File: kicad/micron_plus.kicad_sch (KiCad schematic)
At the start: 0 parts

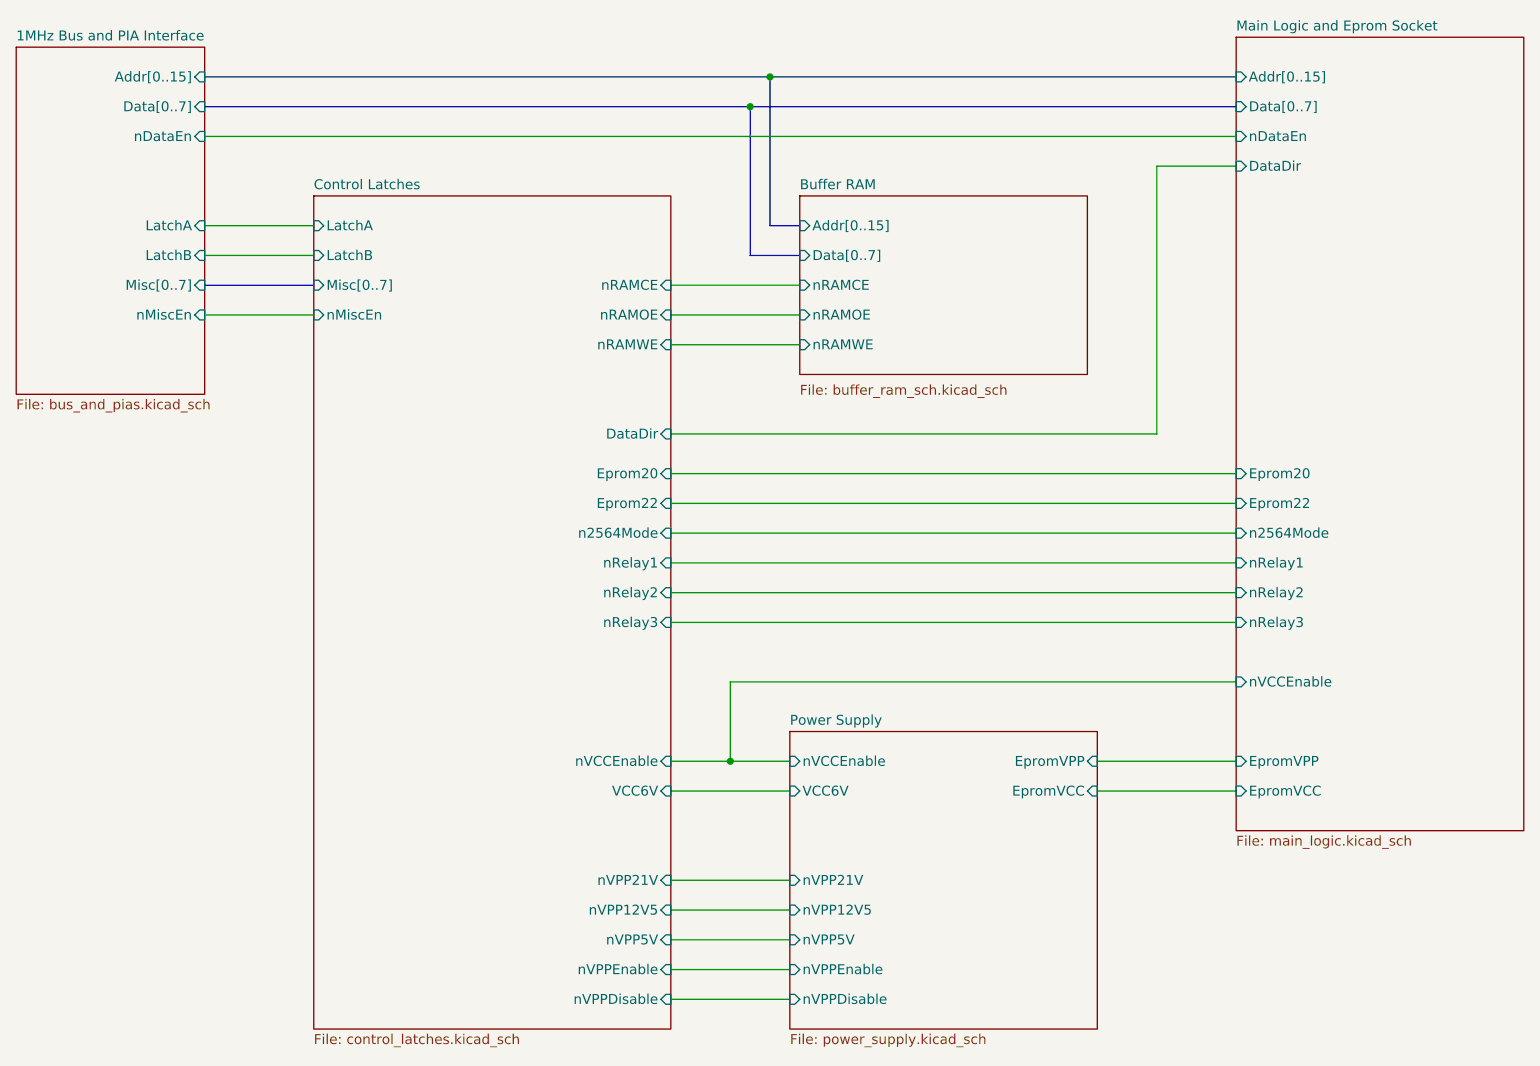
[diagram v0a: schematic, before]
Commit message: Move 7406 onto PSU sheet
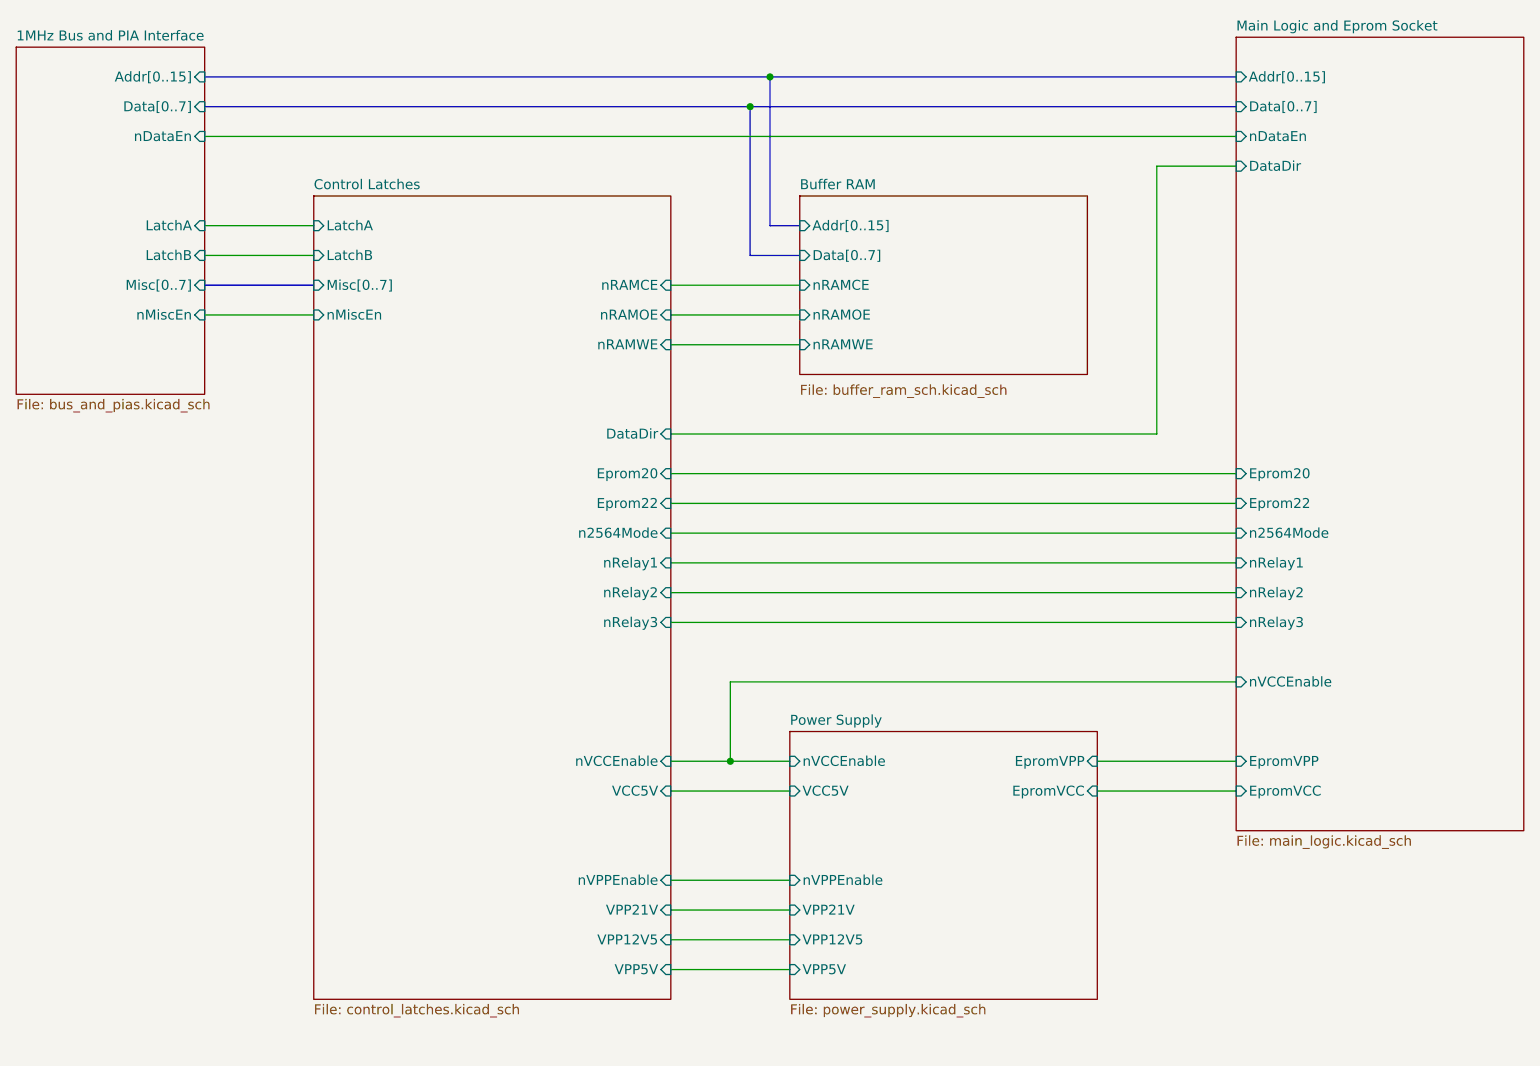
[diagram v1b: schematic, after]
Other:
- sheet Control Latches ports: added VCC5V, VPP12V5, VPP21V, VPP5V; removed VCC6V, nVPP12V5, nVPP21V, nVPP5V, nVPPDisable
- sheet Power Supply ports: added VCC5V, VPP12V5, VPP21V, VPP5V; removed VCC6V, nVPP12V5, nVPP21V, nVPP5V, nVPPDisable
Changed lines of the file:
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@@
-    (stroke (width 0) (type default) (color 0 0 0 0))
-  )
-  (wire (pts (xy 138.43 153.67) (xy 153.67 153.67))
     (stroke (width 0) (type default) (color 0 0 0 0))
   )
@@
     )
   )
-  (sheet (at 92.71 50.8) (size 45.72 106.68) (fields_autoplaced)
+  (sheet (at 92.71 50.8) (size 45.72 102.87) (fields_autoplaced)
     (stroke (width 0.1524) (type solid) (color 0 0 0 0))
     (fill (color 0 0 0 0.0000))
@@
       (effects (font (size 1.27 1.27)) (justify left bottom))
     )
-    (property "Sheet file" "control_latches.kicad_sch" (id 1) (at 92.71 158.0646 0)
+    (property "Sheet file" "control_latches.kicad_sch" (id 1) (at 92.71 154.2546 0)
       (effects (font (size 1.27 1.27)) (justify left top))
     )
@@
       (effects (font (size 1.27 1.27)) (justify right))
     )
-    (pin "nVPPEnable" input (at 138.43 149.86 0)
-      (effects (font (size 1.27 1.27)) (justify right))
-    )
     (pin "LatchB" input (at 92.71 58.42 180)
       (effects (font (size 1.27 1.27)) (justify left))
@@
       (effects (font (size 1.27 1.27)) (justify left))
     )
-    (pin "nVPPDisable" input (at 138.43 153.67 0)
-      (effects (font (size 1.27 1.27)) (justify right))
-    )
     (pin "nVCCEnable" input (at 138.43 123.19 0)
       (effects (font (size 1.27 1.27)) (justify right))
     )
-    (pin "nVPP12V5" input (at 138.43 142.24 0)
-      (effects (font (size 1.27 1.27)) (justify right))
-    )
-    (pin "nVPP21V" input (at 138.43 138.43 0)
-      (effects (font (size 1.27 1.27)) (justify right))
-    )
     (pin "nRelay3" input (at 138.43 105.41 0)
       (effects (font (size 1.27 1.27)) (justify right))
@@
       (effects (font (size 1.27 1.27)) (justify right))
     )
-    (pin "VCC6V" input (at 138.43 127 0)
-      (effects (font (size 1.27 1.27)) (justify right))
-    )
-    (pin "nVPP5V" input (at 138.43 146.05 0)
-      (effects (font (size 1.27 1.27)) (justify right))
-    )
     (pin "Eprom22" input (at 138.43 90.17 0)
       (effects (font (size 1.27 1.27)) (justify right))
     )
-  )
-  (sheet (at 153.67 119.38) (size 39.37 38.1) (fields_autoplaced)
+    (pin "nVPPEnable" input (at 138.43 138.43 0)
+      (effects (font (size 1.27 1.27)) (justify right))
+    )
+    (pin "VPP12V5" input (at 138.43 146.05 0)
+      (effects (font (size 1.27 1.27)) (justify right))
+    )
+    (pin "VPP5V" input (at 138.43 149.86 0)
+      (effects (font (size 1.27 1.27)) (justify right))
+    )
+    (pin "VPP21V" input (at 138.43 142.24 0)
+      (effects (font (size 1.27 1.27)) (justify right))
+    )
+    (pin "VCC5V" input (at 138.43 127 0)
+      (effects (font (size 1.27 1.27)) (justify right))
+    )
+  )
+  (sheet (at 153.67 119.38) (size 39.37 34.29) (fields_autoplaced)
     (stroke (width 0.1524) (type solid) (color 0 0 0 0))
     (fill (color 0 0 0 0.0000))
@@
       (effects (font (size 1.27 1.27)) (justify left bottom))
     )
-    (property "Sheet file" "power_supply.kicad_sch" (id 1) (at 153.67 158.0646 0)
+    (property "Sheet file" "power_supply.kicad_sch" (id 1) (at 153.67 154.2546 0)
       (effects (font (size 1.27 1.27)) (justify left top))
     )
@@
       (effects (font (size 1.27 1.27)) (justify left))
     )
-    (pin "nVPPEnable" input (at 153.67 149.86 180)
-      (effects (font (size 1.27 1.27)) (justify left))
-    )
-    (pin "nVPPDisable" input (at 153.67 153.67 180)
-      (effects (font (size 1.27 1.27)) (justify left))
-    )
     (pin "EpromVPP" input (at 193.04 123.19 0)
       (effects (font (size 1.27 1.27)) (justify right))
@@
       (effects (font (size 1.27 1.27)) (justify right))
     )
-    (pin "nVPP12V5" input (at 153.67 142.24 180)
-      (effects (font (size 1.27 1.27)) (justify left))
-    )
-    (pin "nVPP21V" input (at 153.67 138.43 180)
-      (effects (font (size 1.27 1.27)) (justify left))
-    )
-    (pin "VCC6V" input (at 153.67 127 180)
-      (effects (font (size 1.27 1.27)) (justify left))
-    )
-    (pin "nVPP5V" input (at 153.67 146.05 180)
+    (pin "nVPPEnable" input (at 153.67 138.43 180)
+      (effects (font (size 1.27 1.27)) (justify left))
+    )
+    (pin "VPP5V" input (at 153.67 149.86 180)
+      (effects (font (size 1.27 1.27)) (justify left))
+    )
+    (pin "VPP12V5" input (at 153.67 146.05 180)
+      (effects (font (size 1.27 1.27)) (justify left))
+    )
+    (pin "VPP21V" input (at 153.67 142.24 180)
+      (effects (font (size 1.27 1.27)) (justify left))
+    )
+    (pin "VCC5V" input (at 153.67 127 180)
       (effects (font (size 1.27 1.27)) (justify left))
     )
@@
       (reference "#PWR0130") (unit 1) (value "VCC") (footprint "")
     )
-    (path "/f9a739c5-9b12-47e1-af6a-d12a836d0aef/016a69bd-7efd-4510-9f5e-4c687c8de4a5"
-      (reference "#PWR0131") (unit 1) (value "GND") (footprint "")
-    )
-    (path "/f9a739c5-9b12-47e1-af6a-d12a836d0aef/a183e626-f1a3-4ca3-9306-3481cffa9bd6"
-      (reference "#PWR0132") (unit 1) (value "VCC") (footprint "")
+    (path "/f9d5b6cb-300a-4451-93f6-d466a935f678/c9b2041d-2f8d-4dfc-85d0-5aba6d095277"
+      (reference "#PWR0131") (unit 1) (value "VCC") (footprint "")
+    )
+    (path "/f9d5b6cb-300a-4451-93f6-d466a935f678/5198e16c-d1a4-4b6a-9665-894c686fe876"
+      (reference "#PWR0132") (unit 1) (value "GND") (footprint "")
     )
     (path "/f9a739c5-9b12-47e1-af6a-d12a836d0aef/16db3ad3-b698-4aa3-90b7-04088b9fdf0e"
@@
     )
     (path "/f9d5b6cb-300a-4451-93f6-d466a935f678/02ed6f94-9975-41b5-87d9-9dbd124c6c12"
-      (reference "D4") (unit 1) (value "W005G") (footprint "Diode_THT:Diode_Bridge_Round_D9.8mm")
+      (reference "D4") (unit 1) (value "W005") (footprint "Diode_THT:Diode_Bridge_Round_D9.8mm")
     )
     (path "/f9d5b6cb-300a-4451-93f6-d466a935f678/6c61799b-7692-46f0-9522-e5b5cdff5278"
@@
     )
     (path "/f9d5b6cb-300a-4451-93f6-d466a935f678/cb29e39a-1f72-42a9-92a1-04dc3eb2a1c3"
-      (reference "D10") (unit 1) (value "Green") (footprint "")
+      (reference "D10") (unit 1) (value "Red") (footprint "")
     )
     (path "/f9d5b6cb-300a-4451-93f6-d466a935f678/dce8e02c-3524-4b73-aa4d-e48a7ba074fa"
@@
       (reference "U10") (unit 5) (value "74LS00") (footprint "")
     )
-    (path "/f9a739c5-9b12-47e1-af6a-d12a836d0aef/8ecd197c-e30c-4573-8351-3430b40ffa05"
+    (path "/f9d5b6cb-300a-4451-93f6-d466a935f678/9bbbab92-a748-4a70-b58a-fb1ec0b1e422"
       (reference "U11") (unit 1) (value "7406") (footprint "")
     )
-    (path "/f9a739c5-9b12-47e1-af6a-d12a836d0aef/c754d00c-127f-4f65-9745-87a1d852af81"
+    (path "/f9d5b6cb-300a-4451-93f6-d466a935f678/f3be4064-372e-487a-ad8c-61b660a270ba"
       (reference "U11") (unit 2) (value "7406") (footprint "")
     )
-    (path "/f9a739c5-9b12-47e1-af6a-d12a836d0aef/a3cd5bc0-17b0-4a0c-9950-b088dd683c4a"
+    (path "/f9d5b6cb-300a-4451-93f6-d466a935f678/009fdc9b-db5a-43af-9dd9-441c931a0f02"
       (reference "U11") (unit 3) (value "7406") (footprint "")
     )
-    (path "/f9a739c5-9b12-47e1-af6a-d12a836d0aef/7ab54fa5-de32-4d64-a17b-e72b6b087d13"
+    (path "/f9d5b6cb-300a-4451-93f6-d466a935f678/477355fb-32f5-4364-a273-684cdf4b6918"
       (reference "U11") (unit 4) (value "7406") (footprint "")
     )
-    (path "/f9a739c5-9b12-47e1-af6a-d12a836d0aef/b8a84091-f5c0-4c43-97e6-e27a7301f801"
+    (path "/f9d5b6cb-300a-4451-93f6-d466a935f678/27bb27d4-643b-40db-8806-1f2e6e2e053a"
       (reference "U11") (unit 5) (value "7406") (footprint "")
     )
-    (path "/f9a739c5-9b12-47e1-af6a-d12a836d0aef/61ba8cf2-aaca-4f4e-b748-8a1c4efe1e55"
+    (path "/f9d5b6cb-300a-4451-93f6-d466a935f678/6ba16236-7d16-4401-b3d2-3d96a52ec613"
       (reference "U11") (unit 6) (value "7406") (footprint "")
     )
-    (path "/f9a739c5-9b12-47e1-af6a-d12a836d0aef/b48b5a19-663f-40d4-87c0-ec867f183021"
+    (path "/f9d5b6cb-300a-4451-93f6-d466a935f678/d06ed228-00b9-48c0-83c9-ef7a34ce7790"
       (reference "U11") (unit 7) (value "7406") (footprint "")
     )
@@
     )
     (path "/f9d5b6cb-300a-4451-93f6-d466a935f678/1028567b-e7be-41de-aa18-30638294f7dc"
-      (reference "U19") (unit 1) (value "LM317_TO220") (footprint "Package_TO_SOT_THT:TO-220-3_Vertical")
+      (reference "U19") (unit 1) (value "LM317SP_TO220") (footprint "Package_TO_SOT_THT:TO-220-3_Vertical")
     )
     (path "/f9d5b6cb-300a-4451-93f6-d466a935f678/8bdf432f-fd29-4fde-a11f-6bd24dbabbfb"
